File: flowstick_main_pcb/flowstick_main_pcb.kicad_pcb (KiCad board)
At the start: 4 copper layers, 13 x 24 mm, 53 parts, among them J1 USB_C_Receptacle_USB2.0_16P, J2 Conn_01x01_Pin, J3 Conn_01x01_Pin, J4 Conn_01x01_Pin, J5 Conn_01x01_Pin, SW1 SW_Push, U1 ESP32-S3, U2 MP3414A, U3 LM3671, U4 BQ21040DBV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

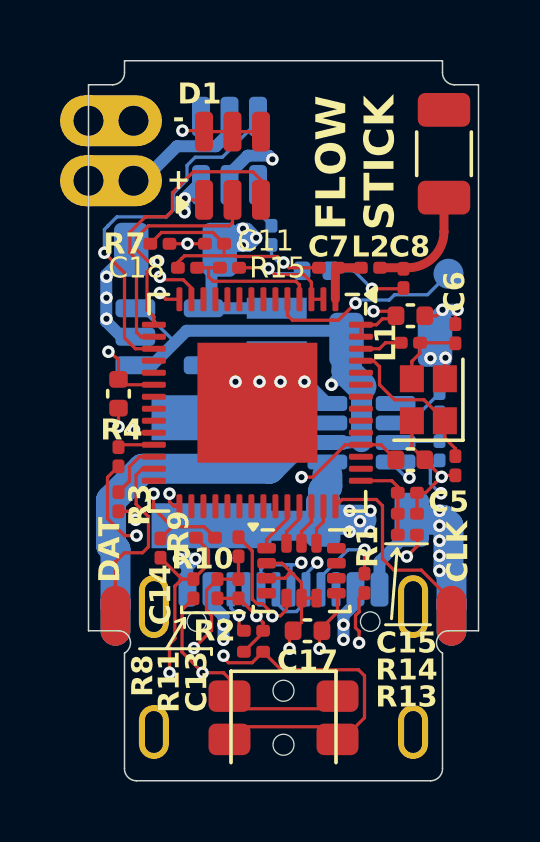
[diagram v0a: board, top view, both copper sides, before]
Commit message: work on rev2 + panelize LED strips
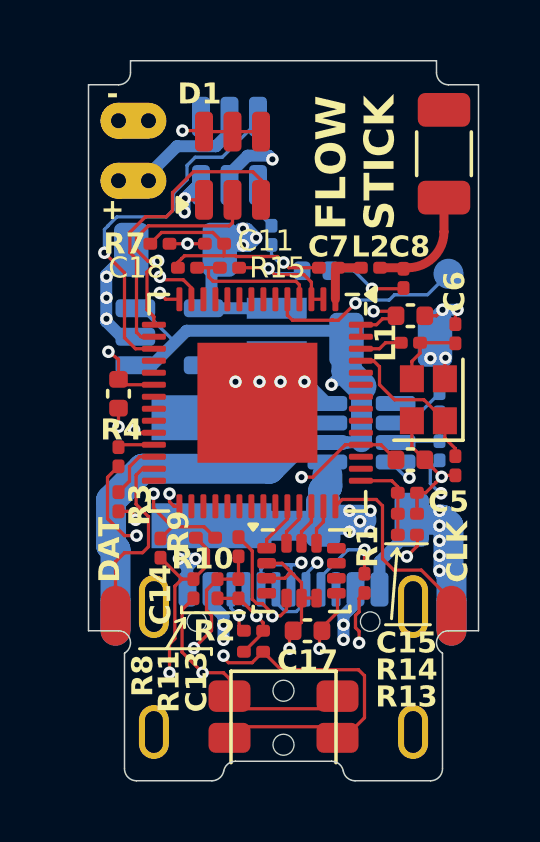
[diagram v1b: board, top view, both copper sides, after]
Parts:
- moved BT1 0.50 mm to (145.5, 80.0)
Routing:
- net +BATT: track 47.0 -> 42.6 mm
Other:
- outline, holes or cut-outs redrawn
- board text added: "rev 2 ~ervanalb"
- board text removed: "rev 1 ~ervanalb"

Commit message: Final rev2, probably
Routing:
- net +BATT: track 42.6 -> 47.2 mm
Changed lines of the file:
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@@
 		(sheetname "/")
 		(sheetfile "flowstick_main_pcb.kicad_sch")
-		(attr smd)
+		(attr smd exclude_from_pos_files exclude_from_bom)
 		(fp_line
 			(start -0.5 0)
@@
 			(layer "F.Fab")
 		)
+		(fp_text user "${REFERENCE}"
+			(at 0 2.5 0)
+			(unlocked yes)
+			(layer "F.Fab")
+			(effects
+				(font
+					(size 1 1)
+					(thickness 0.15)
+				)
+			)
+		)
 		(pad "1" smd oval
 			(at 0 -0.5 90)
 			(size 2 1)
-			(layers "F.Cu" "F.Mask" "F.Paste")
+			(layers "F.Cu" "F.Mask")
 			(net 28 "/LED_CLK")
 			(pinfunction "Pin_1")
@@
 		(sheetname "/")
 		(sheetfile "flowstick_main_pcb.kicad_sch")
-		(attr through_hole)
+		(attr through_hole exclude_from_pos_files exclude_from_bom)
 		(fp_line
 			(start 2 3)
@@
 		(sheetname "/")
 		(sheetfile "flowstick_main_pcb.kicad_sch")
-		(attr smd)
+		(attr smd exclude_from_pos_files exclude_from_bom)
 		(fp_line
 			(start -0.5 0)
@@
 			(layer "F.Fab")
 		)
+		(fp_text user "${REFERENCE}"
+			(at 0 2.5 0)
+			(unlocked yes)
+			(layer "F.Fab")
+			(effects
+				(font
+					(size 1 1)
+					(thickness 0.15)
+				)
+			)
+		)
 		(pad "1" smd oval
 			(at 0 -0.5 90)
 			(size 2 1)
-			(layers "F.Cu" "F.Mask" "F.Paste")
+			(layers "F.Cu" "F.Mask")
 			(net 27 "/LED_DAT")
 			(pinfunction "Pin_1")
@@
 		(sheetname "/")
 		(sheetfile "flowstick_main_pcb.kicad_sch")
-		(attr smd)
+		(attr smd exclude_from_pos_files exclude_from_bom)
 		(fp_line
 			(start -0.5 0)
@@
 			(at 0 0.5 90)
 			(size 2 1)
-			(layers "B.Cu" "B.Mask" "B.Paste")
+			(layers "B.Cu" "B.Mask")
 			(net 1 "GND")
 			(pinfunction "Pin_1")
@@
 		(sheetname "/")
 		(sheetfile "flowstick_main_pcb.kicad_sch")
-		(attr smd)
+		(attr smd exclude_from_pos_files exclude_from_bom)
 		(fp_line
 			(start -0.5 0)
@@
 			(layer "B.Fab")
 		)
+		(fp_text user "${REFERENCE}"
+			(at 0 -2.5 0)
+			(unlocked yes)
+			(layer "B.Fab")
+			(effects
+				(font
+					(size 1 1)
+					(thickness 0.15)
+				)
+				(justify mirror)
+			)
+		)
 		(pad "1" smd oval
 			(at 0 0.5 90)
 			(size 2 1)
-			(layers "B.Cu" "B.Mask" "B.Paste")
+			(layers "B.Cu" "B.Mask")
 			(net 8 "+5V")
 			(pinfunction "Pin_1")
@@
 		(sheetname "/")
 		(sheetfile "flowstick_main_pcb.kicad_sch")
-		(attr exclude_from_pos_files)
+		(attr exclude_from_pos_files exclude_from_bom)
 		(fp_circle
 			(center 0 0)
@@
 	)
 	(segment
+		(start 144.979 82.121)
+		(end 145.5 81.6)
+		(width 1)
+		(layer "In2.Cu")
+		(net 3)
+	)
+	(segment
 		(start 146.619 95.711248)
 		(end 146.619 94.491621)
@@
 	)
 	(segment
+		(start 144.979 84.379)
+		(end 144.979 82.121)
+		(width 1)
+		(layer "In2.Cu")
+		(net 3)
+	)
+	(segment
 		(start 147.3 96.4)
 		(end 147.3 96.392248)
@@
 		(width 1)
 		(layer "In2.Cu")
+		(net 3)
+	)
+	(segment
+		(start 145.5 81.6)
+		(end 145.5 80)
+		(width 1)
+		(layer "In2.Cu")
